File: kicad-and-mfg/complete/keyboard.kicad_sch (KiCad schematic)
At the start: 74 parts, among them P2 KEYB CONN 1

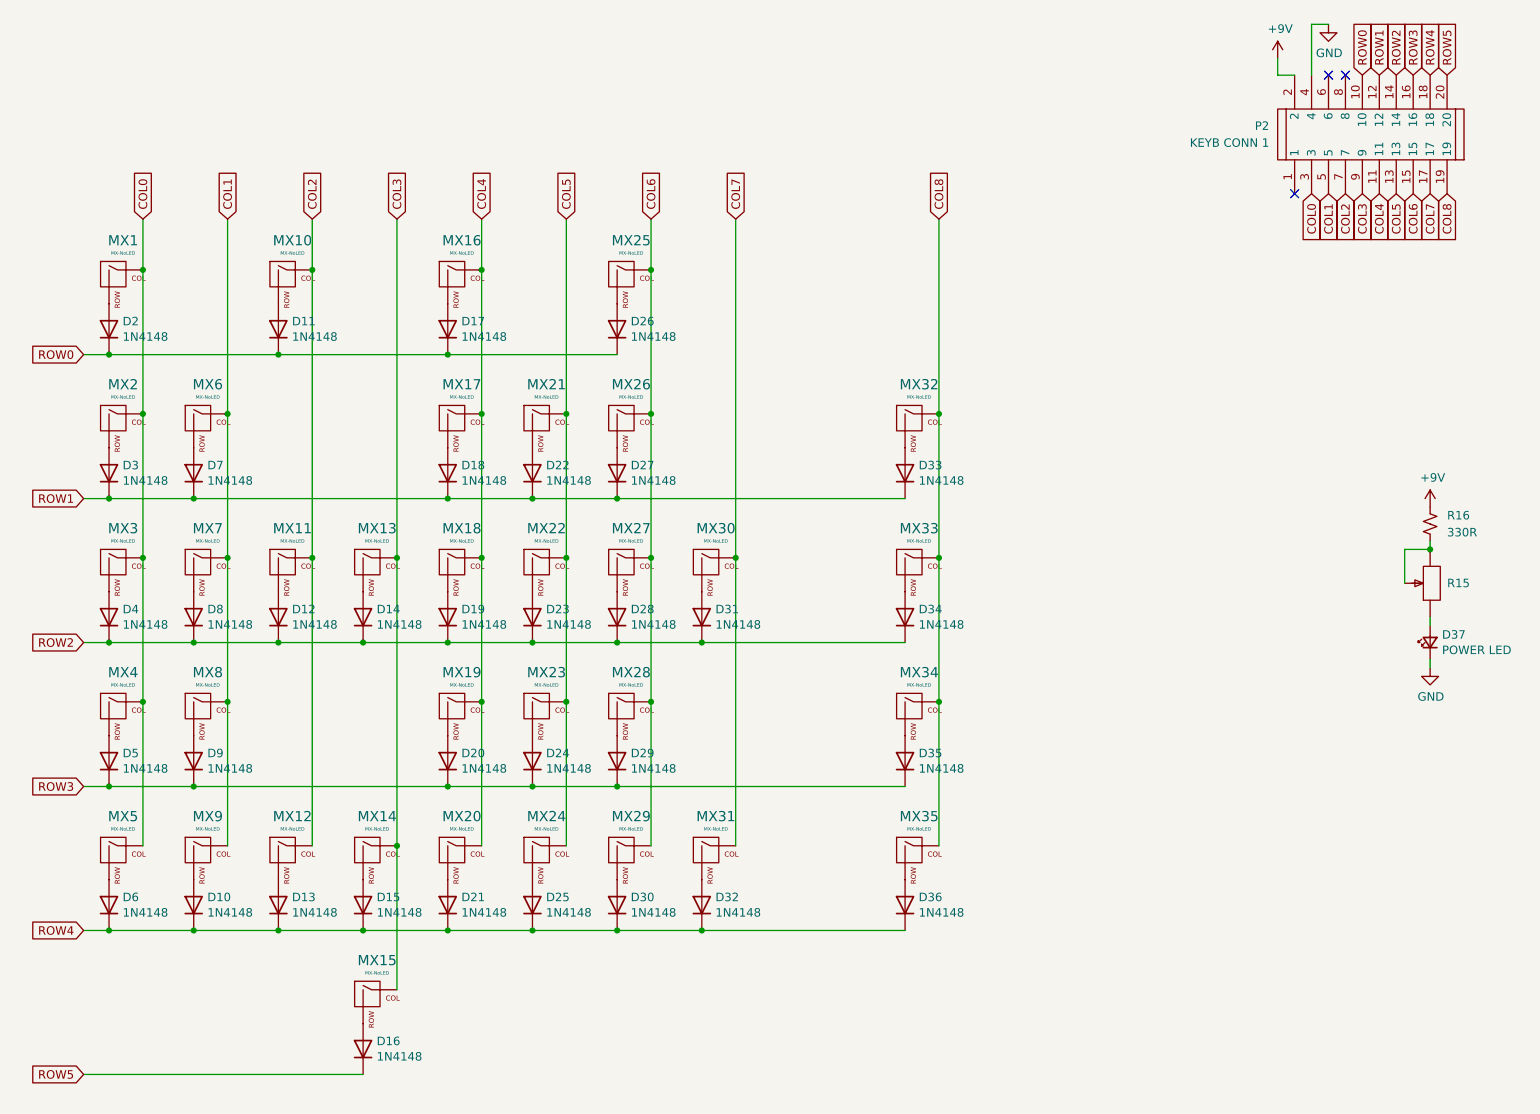
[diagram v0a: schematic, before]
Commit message: changeed path, migrated to kicad 10
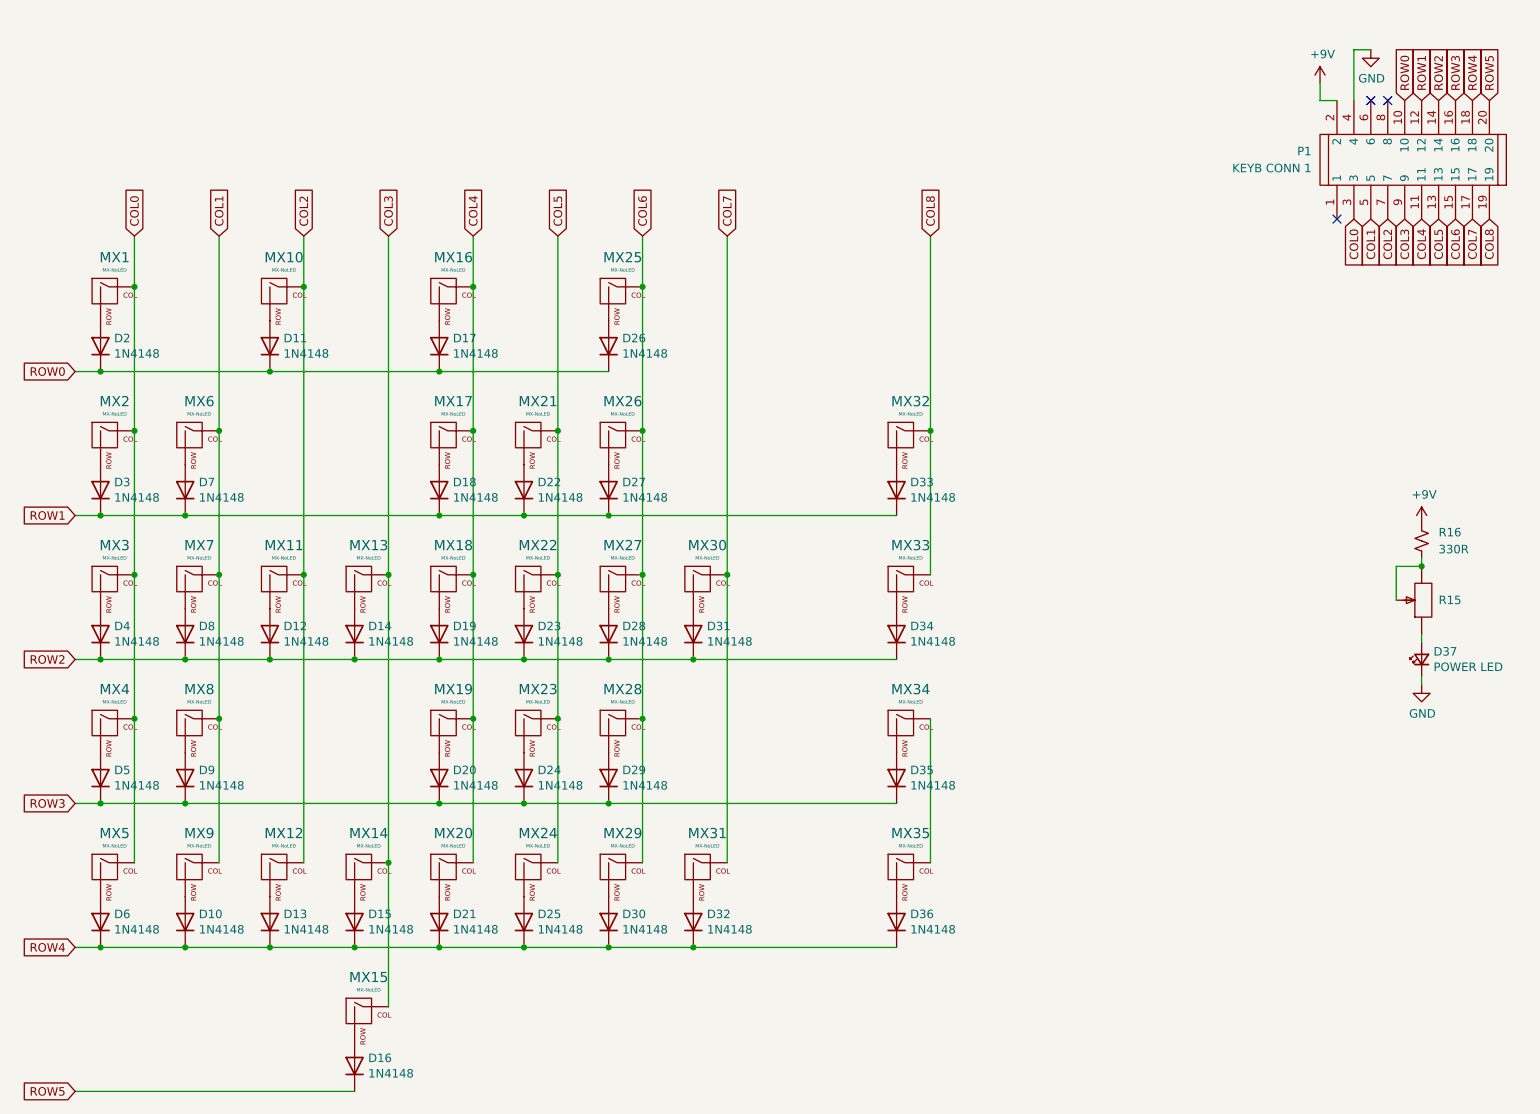
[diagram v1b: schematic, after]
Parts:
- removed P2: KEYB CONN 1, EasyEDA_Lib:IDC-TH_20P-L33.0-W13.8-H-M-R2-C10-P2.54-S2.54-TR, symbol EasyEDA_Lib:IDC Box 2X10 2.54MM
- added P1: KEYB CONN 1, EasyEDA_Lib:IDC-TH_20P-L33.0-W13.8-H-M-R2-C10-P2.54-S2.54-TR, symbol EasyEDA_Lib:IDC Box 2X10 2.54MM
- D10, D11, D12, D13, D14, D15, D16, D17, D18, D19, D2, D20, D21, D22, D23, D24, D25, D26, D27, D28, D29, D3, D30, D31, D32, D33, D34, D35, D36, D4, D5, D6, D7, D8, D9: footprint EasyEDA_Lib:SOD-523_L1.2-W0.8-LS1.6-RD-1 -> Diode_THT:D_DO-35_SOD27_P7.62mm_Horizontal
- MX1, MX10, MX11, MX12, MX13, MX14, MX16, MX17, MX18, MX19, MX2, MX20, MX21, MX22, MX23, MX24, MX25, MX26, MX27, MX28, MX29, MX3, MX30, MX31, MX32, MX33, MX34, MX35, MX4, MX5, MX6, MX7, MX8, MX9: footprint clholm-kicad-library:MX-Hotswap-1U -> cholm-footprints:MXOnly-1U-NoLED
- MX15: footprint clholm-kicad-library:MX-Hotswap-2.25U -> cholm-footprints:MXOnly-2.25U-NoLED
- R16: footprint EasyEDA_Lib:R0805 -> (none)
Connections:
- net +9V: now also P1.2
- net COL0: now also P1.3
- net COL1: now also P1.5
- net COL2: now also P1.7
- net COL3: now also P1.9
- net COL4: now also P1.11
- net COL5: now also P1.13
- net COL6: now also P1.15
- net COL7: now also P1.17
- net COL8: now also P1.19; no longer MX34.1 (COL), MX35.1 (COL)
- net GND: now also P1.4
- net ROW0: now also P1.10
- net ROW1: now also P1.12
- net ROW2: now also P1.14
- net ROW3: now also P1.16
- net ROW4: now also P1.18
- net ROW5: now also P1.20
- new net: MX34.1 (COL), MX35.1 (COL)
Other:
- moved on the sheet: D10, D11, D12, D13, D14, D15, D16, D17, D18, D19, D2, D20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
